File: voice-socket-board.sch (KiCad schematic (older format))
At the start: 302 parts, among them J1 JACK_MONO_SW, J2 JACK_MONO_SW, J3 JACK_MONO_SW, P1 CONN_01X03, P2 CONN_01X03, P3 CONN_02X05, P4 DDR3-DIMM, Q1 MMBT3904, Q10 MMBT3906, Q2 DMMT3904W, Q3 2N7002, Q4 2N7002, Q6 MMBT3906, Q7 MMBT3904, Q8 MMBT3904, Q9 MMBT3904, SW1 SPST, SW10 SP3T, SW11 SP3T, SW12 SP3T, SW13 SP3T, SW14 SPST, SW15 TACT_SWITCH, SW16 SP3T, SW2 SPST, SW3 SP3T, SW4 SP3T, SW5 SPST, SW6 SPST, SW7 Switch_SPDT_x2, SW8 2P3T, SW9 SP3T, U1 LM833, U10 TL072-, U11 NE5534, U12 TL072-, U2 TL072-, U3 TL072-, U4 TL072-, U5 TL072-, U6 TL072-, U7 MAX9945, U8 CD4013, U9 TL072-

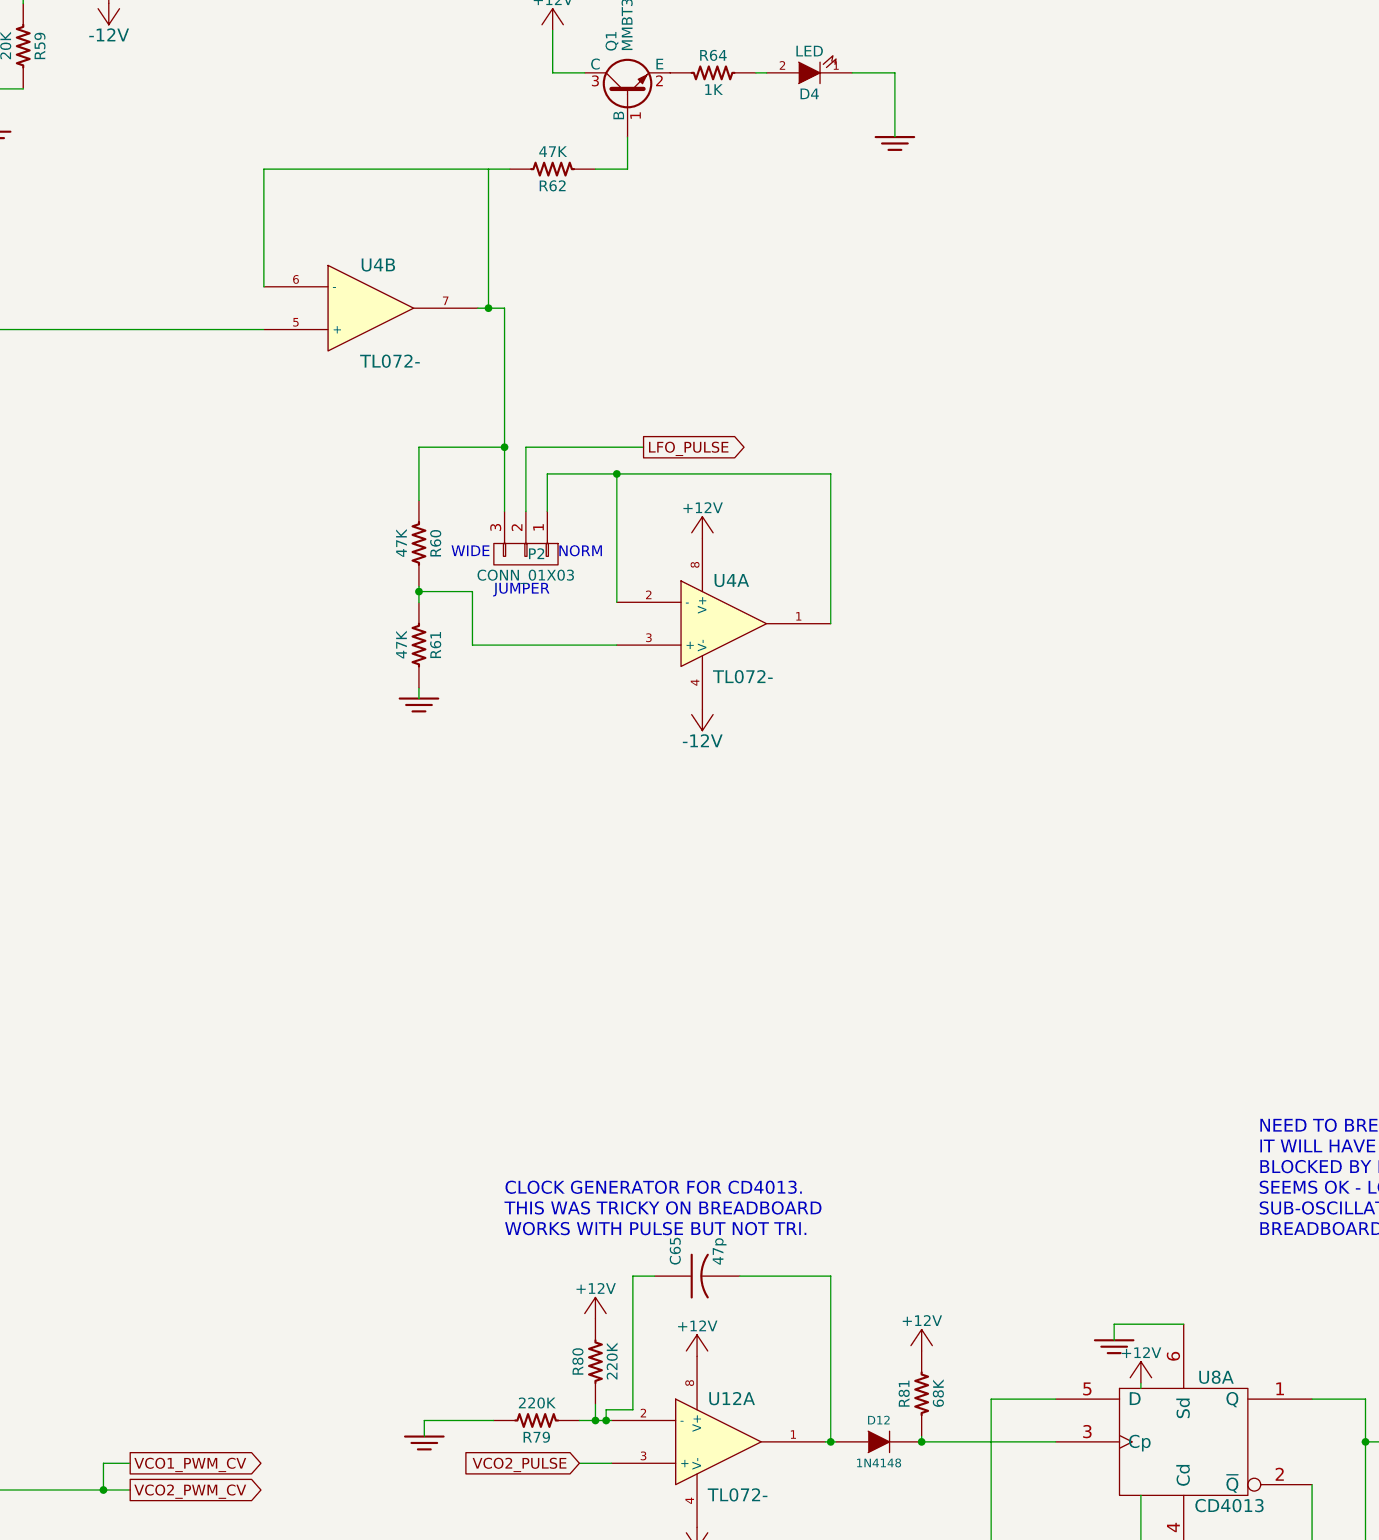
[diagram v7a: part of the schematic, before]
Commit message: fixed a board level error where sub oscillator intermediate clock was shorted to sub oscillator output test pin. added a couple of notes in schematic for corrections that still need to be made
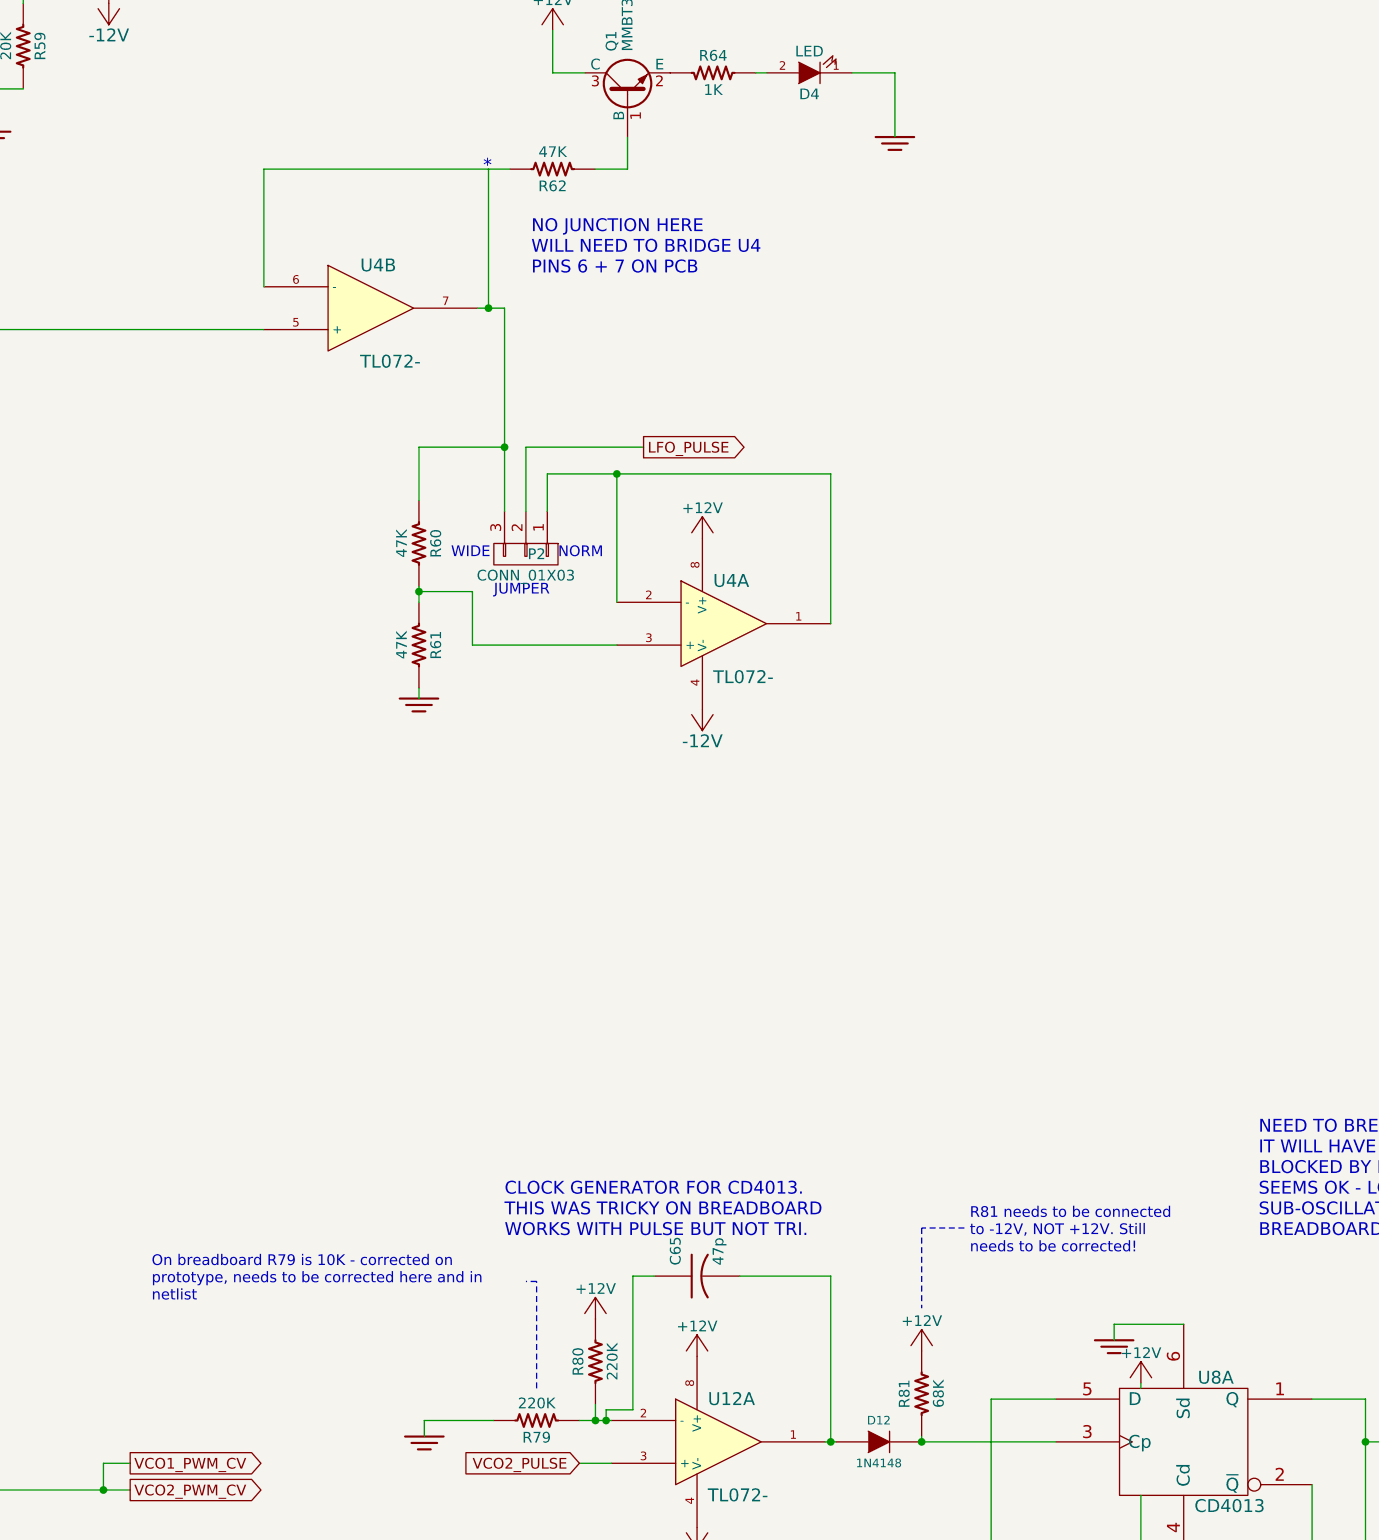
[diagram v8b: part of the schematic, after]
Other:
- note added: "*"
- note added: "NO JUNCTION HERE\nWILL NEED TO BRIDGE U4 \nPINS 6 + 7 ON PCB"
- note added: "On breadboard R79 is 10K - corrected on \nprototype, needs to be corrected here and in\nnetlist"
- note added: "R81 needs to be connected\nto -12V, NOT +12V. Still\nneeds to be corrected!"
